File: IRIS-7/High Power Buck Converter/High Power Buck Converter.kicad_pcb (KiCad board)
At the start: 2 copper layers, 37 parts, among them IC1 LM5088-2, P1 ST-2.54, P2 ST-2.54, P3 ST-2.54, P4 ST-2.54, Q1 CSD19534Q5A

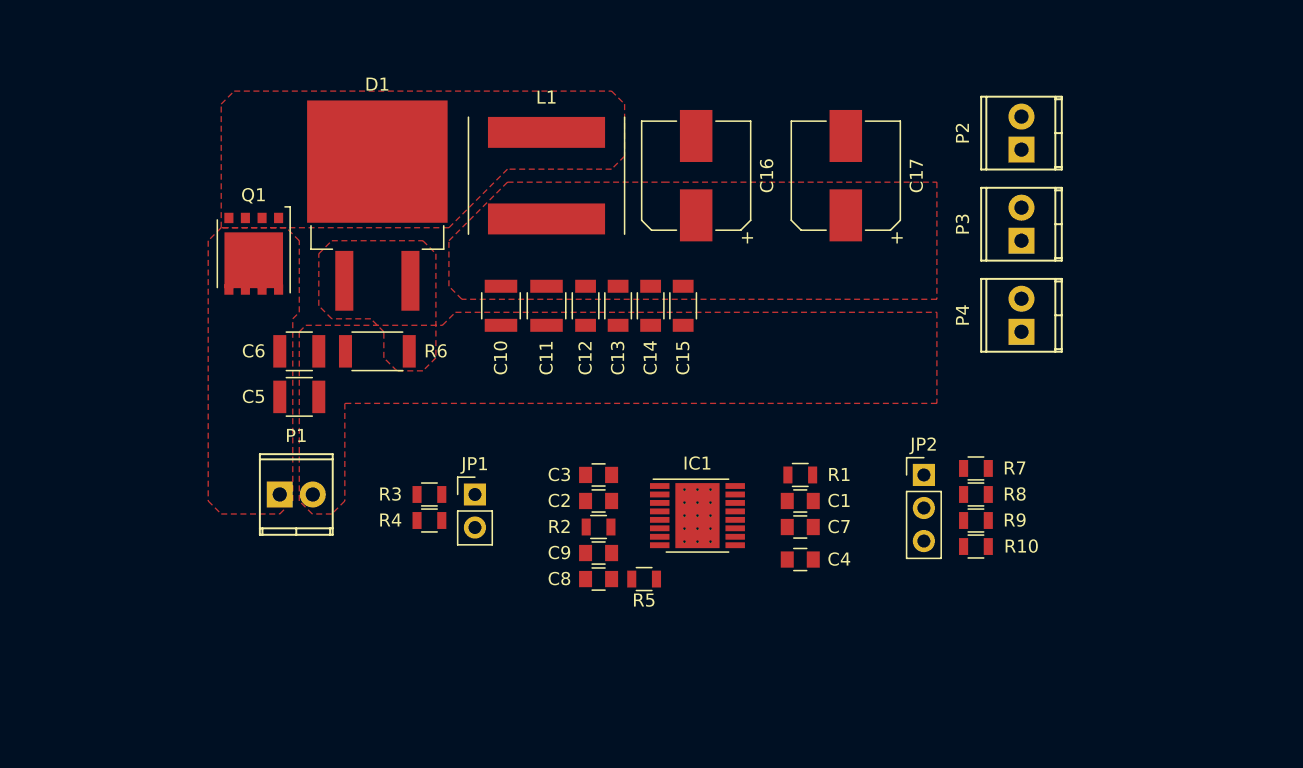
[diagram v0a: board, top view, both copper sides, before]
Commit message: Update power routing
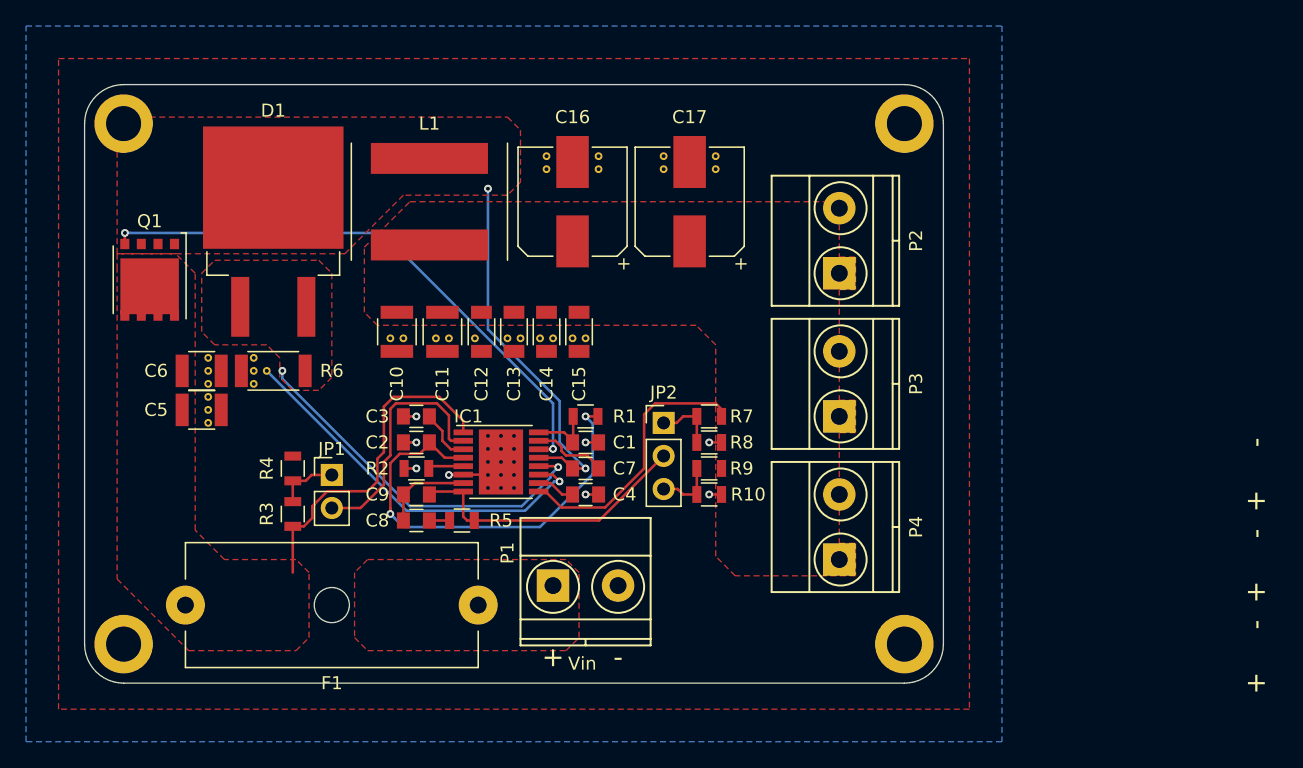
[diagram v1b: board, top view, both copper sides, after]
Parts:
- added F1: 3.5A, Fuse_Holders_and_Fuses:Fuseholder5x20_horiz_open_Schurter_0031_8201, F.Cu at (112.2, 102.0)
- added REF**: VIA_0.3_0.6, Buck_Converter:VIA_0.3_0.6, F.Cu at (95.0, 83.0)
- added REF**: VIA_0.3_0.6, Buck_Converter:VIA_0.3_0.6, F.Cu at (126.5, 67.5)
- added REF**: VIA_0.3_0.6, Buck_Converter:VIA_0.3_0.6, F.Cu at (121.5, 68.5)
- added REF**: VIA_0.3_0.6, Buck_Converter:VIA_0.3_0.6, F.Cu at (121.5, 67.5)
- added REF**: VIA_0.3_0.6, Buck_Converter:VIA_0.3_0.6, F.Cu at (117.5, 68.5)
- added REF**: VIA_0.3_0.6, Buck_Converter:VIA_0.3_0.6, F.Cu at (117.5, 67.5)
- added REF**: VIA_0.3_0.6, Buck_Converter:VIA_0.3_0.6, F.Cu at (120.5, 81.5)
- added REF**: VIA_0.3_0.6, Buck_Converter:VIA_0.3_0.6, F.Cu at (119.5, 81.5)
- added REF**: VIA_0.3_0.6, Buck_Converter:VIA_0.3_0.6, F.Cu at (118.0, 81.5)
- added REF**: VIA_0.3_0.6, Buck_Converter:VIA_0.3_0.6, F.Cu at (117.0, 81.5)
- added REF**: VIA_0.3_0.6, Buck_Converter:VIA_0.3_0.6, F.Cu at (115.5, 81.5)
- added REF**: VIA_0.3_0.6, Buck_Converter:VIA_0.3_0.6, F.Cu at (95.0, 85.0)
- added REF**: VIA_0.3_0.6, Buck_Converter:VIA_0.3_0.6, F.Cu at (114.5, 81.5)
- added REF**: VIA_0.3_0.6, Buck_Converter:VIA_0.3_0.6, F.Cu at (112.0, 81.5)
- added REF**: VIA_0.3_0.6, Buck_Converter:VIA_0.3_0.6, F.Cu at (110.0, 81.5)
- added REF**: VIA_0.3_0.6, Buck_Converter:VIA_0.3_0.6, F.Cu at (109.0, 81.5)
- added REF**: VIA_0.3_0.6, Buck_Converter:VIA_0.3_0.6, F.Cu at (106.5, 81.5)
- added REF**: VIA_0.3_0.6, Buck_Converter:VIA_0.3_0.6, F.Cu at (105.5, 81.5)
- added REF**: VIA_0.3_0.6, Buck_Converter:VIA_0.3_0.6, F.Cu at (95.0, 84.0)
- added REF**: VIA_0.3_0.6, Buck_Converter:VIA_0.3_0.6, F.Cu at (91.5, 85.0)
- added REF**: VIA_0.3_0.6, Buck_Converter:VIA_0.3_0.6, F.Cu at (91.5, 87.0)
- added REF**: VIA_0.3_0.6, VIA_0.3_0.6, F.Cu at (96.0, 84.0)
- added REF**: VIA_0.3_0.6, Buck_Converter:VIA_0.3_0.6, F.Cu at (91.5, 88.0)
- added REF**: MountingHole_2.7mm_M2.5_ISO7380_Pad, Mounting_Holes:MountingHole_2.7mm_M2.5_ISO7380_Pad, F.Cu at (145.0, 65.0)
- added REF**: MountingHole_2.7mm_M2.5_ISO7380_Pad, Mounting_Holes:MountingHole_2.7mm_M2.5_ISO7380_Pad, F.Cu at (145.0, 105.0)
- added REF**: MountingHole_2.7mm_M2.5_ISO7380_Pad, Mounting_Holes:MountingHole_2.7mm_M2.5_ISO7380_Pad, F.Cu at (85.0, 105.0)
- added REF**: MountingHole_2.7mm_M2.5_ISO7380_Pad, Mounting_Holes:MountingHole_2.7mm_M2.5_ISO7380_Pad, F.Cu at (85.0, 65.0)
- added REF**: VIA_0.3_0.6, Buck_Converter:VIA_0.3_0.6, F.Cu at (91.5, 86.0)
- added REF**: VIA_0.3_0.6, Buck_Converter:VIA_0.3_0.6, F.Cu at (91.5, 83.0)
- added REF**: VIA_0.3_0.6, Buck_Converter:VIA_0.3_0.6, F.Cu at (91.5, 84.0)
- added REF**: VIA_0.3_0.6, Buck_Converter:VIA_0.3_0.6, F.Cu at (130.5, 68.5)
- added REF**: VIA_0.3_0.6, Buck_Converter:VIA_0.3_0.6, F.Cu at (130.5, 67.5)
- added REF**: VIA_0.3_0.6, Buck_Converter:VIA_0.3_0.6, F.Cu at (126.5, 68.5)
- P1, P2, P3, P4: footprint Terminal_Blocks:TerminalBlock_Pheonix_MPT-2.54mm_2pol -> Terminal_Blocks:TerminalBlock_Pheonix_MKDS1.5-2pol
- moved P4 22.4 mm to (140.0, 98.5)
- moved P1 22.1 mm to (118.0, 100.5)
- moved R10 20.9 mm to (130.0, 93.5)
- moved R7 20.9 mm to (130.0, 87.5)
- moved R8 20.9 mm to (130.0, 89.5)
- moved R9 20.9 mm to (130.0, 91.5)
- moved JP2 20.4 mm to (126.5, 88.0)
- moved P3 19.4 mm to (140.0, 87.5)
- moved C4 17.2 mm to (120.5, 93.5)
- moved C1 17.1 mm to (120.5, 89.5)
- moved C7 17.1 mm to (120.5, 91.5)
- moved R1 17.1 mm to (120.5, 87.5)
- moved P2 16.9 mm to (140.0, 76.5)
- moved IC1 15.7 mm to (114.0, 91.0)
- moved C2 14.7 mm to (107.5, 89.5)
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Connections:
- IC1 pad 11: GND -> (no net)
- P1 pad 1: /Vin -> /Vbatt
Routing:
- net /HG: track 0.00 -> 43.8 mm, vias 0 -> 2
- net /RAMP: track 0.00 -> 34.0 mm, vias 0 -> 2
- net (no net): track 0.00 -> 29.7 mm, vias 0 -> 1
- net /CS: track 0.00 -> 28.8 mm, vias 0 -> 2
- net /SW: track 0.00 -> 28.5 mm, vias 0 -> 2
- net /Vin: track 0.00 -> 26.0 mm
- net /FB: track 0.00 -> 22.2 mm
- net /Vout: track 0.00 -> 21.0 mm
- net /EN: track 0.00 -> 18.8 mm
- net GND: track 0.00 -> 9.91 mm, vias 0 -> 8
- net /COMP: track 0.00 -> 6.96 mm
- net Net-(C7-Pad1): track 0.00 -> 5.74 mm
- net /VCC: track 0.00 -> 5.01 mm
- net /EN_UVLO: track 0.00 -> 4.79 mm
- net /FB_12V: track 0.00 -> 4.76 mm
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- added copper zone on F.Cu, net /Vbatt
- added copper zone on B.Cu, net GND
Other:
- board outline added: 66 x 46 mm
- net class Default: clearance 0.2 -> 0.15; trace_width 0.25 -> 0.2; via_drill 0.4 -> 0.3
- rule trace_clearance: 0.2 -> 0.15
- board text added: "+"
- board text added: "-"
- board text added: "TODO: - Add input fuse - Board label text - IRIS logo - More gnd coupling vias"
- board text added: "Vin"

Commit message: Finish layout and final tweaks
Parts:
- removed the REF** at (95.0, 83.0)
- removed the REF** at (126.5, 67.5)
- removed the REF** at (121.5, 68.5)
- removed the REF** at (121.5, 67.5)
- removed the REF** at (117.5, 68.5)
- removed the REF** at (117.5, 67.5)
- removed the REF** at (120.5, 81.5)
- removed the REF** at (119.5, 81.5)
- removed the REF** at (118.0, 81.5)
- removed the REF** at (117.0, 81.5)
- removed the REF** at (115.5, 81.5)
- removed the REF** at (95.0, 85.0)
- removed the REF** at (114.5, 81.5)
- removed the REF** at (112.0, 81.5)
- removed the REF** at (110.0, 81.5)
- removed the REF** at (109.0, 81.5)
- removed the REF** at (106.5, 81.5)
- removed the REF** at (105.5, 81.5)
- removed the REF** at (95.0, 84.0)
- removed the REF** at (91.5, 85.0)
- removed the REF** at (91.5, 87.0)
- removed the REF** at (96.0, 84.0)
- removed the REF** at (91.5, 88.0)
- removed the REF** at (91.5, 86.0)
- removed the REF** at (91.5, 83.0)
- removed the REF** at (91.5, 84.0)
- removed the REF** at (130.5, 68.5)
- removed the REF** at (130.5, 67.5)
- removed the REF** at (126.5, 68.5)
- added D2: Led_Small, LEDs:LED_0805, F.Cu at (130.5, 66.0)
- added G***: LOGO, IRIS_Logos:IRIS_Logo_9.2, F.Cu at (87.5, 79.0)
- added J2: CS_P, Buck_Converter:SMD_0.3, F.Cu at (102.7, 92.5)
- added R11: 34.8k, Resistors_SMD:R_0805, F.Cu at (126.5, 66.0)
- added REF**: VIA_0.3_0.6, Buck_Converter:VIA_0.3_0.6, F.Cu at (132.0, 72.8)
- added REF**: VIA_0.3_0.6, Buck_Converter:VIA_0.3_0.6, F.Cu at (123.2, 88.8)
- added REF**: VIA_0.3_0.6, Buck_Converter:VIA_0.3_0.6, F.Cu at (122.0, 88.8)
- added REF**: VIA_0.3_0.6, Buck_Converter:VIA_0.3_0.6, F.Cu at (121.0, 88.8)
- added REF**: VIA_0.3_0.6, Buck_Converter:VIA_0.3_0.6, F.Cu at (119.8, 88.8)
- added REF**: VIA_0.3_0.6, Buck_Converter:VIA_0.3_0.6, F.Cu at (118.8, 88.8)
- added REF**: VIA_0.3_0.6, Buck_Converter:VIA_0.3_0.6, F.Cu at (117.5, 88.8)
- added REF**: VIA_0.3_0.6, Buck_Converter:VIA_0.3_0.6, F.Cu at (116.5, 88.8)
- added REF**: VIA_0.3_0.6, Buck_Converter:VIA_0.3_0.6, F.Cu at (113.2, 88.8)
- added REF**: VIA_0.3_0.6, Buck_Converter:VIA_0.3_0.6, F.Cu at (115.2, 88.8)
- added REF**: VIA_0.3_0.6, Buck_Converter:VIA_0.3_0.6, F.Cu at (114.2, 88.8)
- added REF**: VIA_0.3_0.6, Buck_Converter:VIA_0.3_0.6, F.Cu at (128.0, 71.8)
- added REF**: VIA_0.3_0.6, Buck_Converter:VIA_0.3_0.6, F.Cu at (112.2, 88.8)
- added REF**: VIA_0.3_0.6, Buck_Converter:VIA_0.3_0.6, F.Cu at (111.2, 88.8)
- added REF**: VIA_0.3_0.6, Buck_Converter:VIA_0.3_0.6, F.Cu at (110.2, 88.8)
- added REF**: VIA_0.3_0.6, Buck_Converter:VIA_0.3_0.6, F.Cu at (95.5, 95.8)
- added REF**: VIA_0.3_0.6, Buck_Converter:VIA_0.3_0.6, F.Cu at (95.5, 93.8)
- added REF**: VIA_0.3_0.6, Buck_Converter:VIA_0.3_0.6, F.Cu at (95.5, 94.8)
- added REF**: VIA_0.3_0.6, Buck_Converter:VIA_0.3_0.6, F.Cu at (95.5, 92.8)
- added REF**: VIA_0.3_0.6, Buck_Converter:VIA_0.3_0.6, F.Cu at (95.5, 90.8)
- added REF**: VIA_0.3_0.6, Buck_Converter:VIA_0.3_0.6, F.Cu at (132.0, 71.8)
- added REF**: VIA_0.3_0.6, Buck_Converter:VIA_0.3_0.6, F.Cu at (95.5, 91.8)
- added REF**: VIA_0.3_0.6, Buck_Converter:VIA_0.3_0.6, F.Cu at (128.0, 72.8)
- added REF**: VIA_0.3_0.6, Buck_Converter:VIA_0.3_0.6, F.Cu at (132.0, 89.8)
- added REF**: VIA_0.3_0.6, Buck_Converter:VIA_0.3_0.6, F.Cu at (132.0, 88.8)
- added REF**: VIA_0.3_0.6, Buck_Converter:VIA_0.3_0.6, F.Cu at (128.0, 89.8)
- added REF**: VIA_0.3_0.6, Buck_Converter:VIA_0.3_0.6, F.Cu at (128.0, 88.8)
- added REF**: VIA_0.3_0.6, Buck_Converter:VIA_0.3_0.6, F.Cu at (124.2, 88.8)
- moved C1 25.9 mm to (109.5, 66.0)
- moved C2 25.9 mm to (96.5, 66.0)
- moved C3 25.9 mm to (96.5, 64.0)
- moved C4 25.9 mm to (109.5, 70.0)
- moved C7 25.9 mm to (109.5, 68.0)
- moved C8 25.9 mm to (96.5, 72.0)
- moved C9 25.9 mm to (96.5, 70.0)
- moved IC1 25.9 mm to (103.0, 67.5)
- moved R1 25.9 mm to (109.5, 64.0)
- moved R2 25.9 mm to (96.5, 68.0)
- moved R5 25.9 mm to (100.0, 72.0)
- moved JP1 24.8 mm to (90.5, 69.5)
- moved R3 24.8 mm to (87.5, 72.5)
- moved R4 24.8 mm to (87.5, 69.0)
- moved JP2 23.2 mm to (117.8, 66.5)
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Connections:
- net /CS renamed /CS_P
- IC1 pad 11: (no net) -> /CS_N
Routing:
- net /CS_N: track 0.00 -> 33.1 mm, vias 0 -> 2
- net (no net): track 29.7 -> 0.00 mm, vias 1 -> 0
- net /SW: track 28.5 -> 12.3 mm
- net /RAMP: track 34.0 -> 18.9 mm
- net /HG: track 43.8 -> 31.0 mm
- net /EN: track 18.8 -> 12.2 mm, vias 0 -> 1
- net /CS_P: track 28.8 -> 34.3 mm
- net /Vin: track 26.0 -> 30.1 mm, vias 0 -> 2
- net /Vout: track 21.0 -> 23.6 mm
- net Net-(D2-Pad2): track 0.00 -> 1.95 mm
- net /FB: track 22.2 -> 23.6 mm
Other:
- net class Default: clearance 0.15 -> 0.2
- rule pad_to_mask_clearance: 0 -> 0.05
- rule trace_clearance: 0.15 -> 0.2
- board text added: "-V"
- board text added: "12V"
- board text added: "24V"
- board text added: "Buck Converter"
- board text added: "Byron Hopps"
- board text added: "IN"
- board text added: "JP1-UVLO Short: EN"
- board text added: "Notes"
- board text added: "OUT"
- board text added: "Please place any manufacturing marks in this area"
- board text added: "Rev A, April 2017"
- board text added: "Serial #"
- board text added: "TH"
- board text added: "V"
- board text removed: "TODO: - Add input fuse - Board label text - IRIS logo - More gnd coupling vias"
- board text removed: "Vin"
